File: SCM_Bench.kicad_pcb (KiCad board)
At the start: 4 copper layers, 86 x 145 mm, 330 parts, among them J101 Conn_Coaxial, J102 Conn_Coaxial, J103 Conn_Coaxial, J104 Conn_Coaxial, J105 Conn_Coaxial, J106 Conn_Coaxial, J107 Conn_02x20_Odd_Even, J108 Conn_02x07_Odd_Even, J109 Conn_02x07_Odd_Even, J1601 Conn_01x06, J301 RF_Shield_One_Piece, J401 RF_Shield_One_Piece, J501 RF_Shield_One_Piece, J601 RF_Shield_One_Piece, J701 RF_Shield_One_Piece, J801 RF_Shield_One_Piece, J901 Conn_Coaxial, J902 Conn_Coaxial, J903 Conn_Coaxial, J904 Conn_Coaxial, SW101 SW_Push, U1001 AD9747BCPZ, U1002 SN65LVDS1DBV, U101 ASDMB-xxxMHz, U1101 AD8021, U1201 AD8021, U1301 AD9747BCPZ, U1302 SN65LVDS1DBV, U1401 AD8021, U1501 AD8021, U1601 ICE40HX1K-4K-TQ144, U1602 M25PX32-VMW, U1701 tps6240x, U301 LT6600IS8, U302 LTC2386-18, U303 SN65LVDS1050PW, U401 LT6600IS8, U402 LTC2386-18, U403 SN65LVDS1050PW, U501 LT6600IS8, U502 LTC2386-18, U503 SN65LVDS1050PW, U601 LT6600IS8, U602 LTC2386-18, U603 SN65LVDS1050PW, U701 LT6600IS8, U702 LTC2386-18, U703 SN65LVDS1050PW, U801 LT6600IS8, U802 LTC2386-18, U803 SN65LVDS1050PW

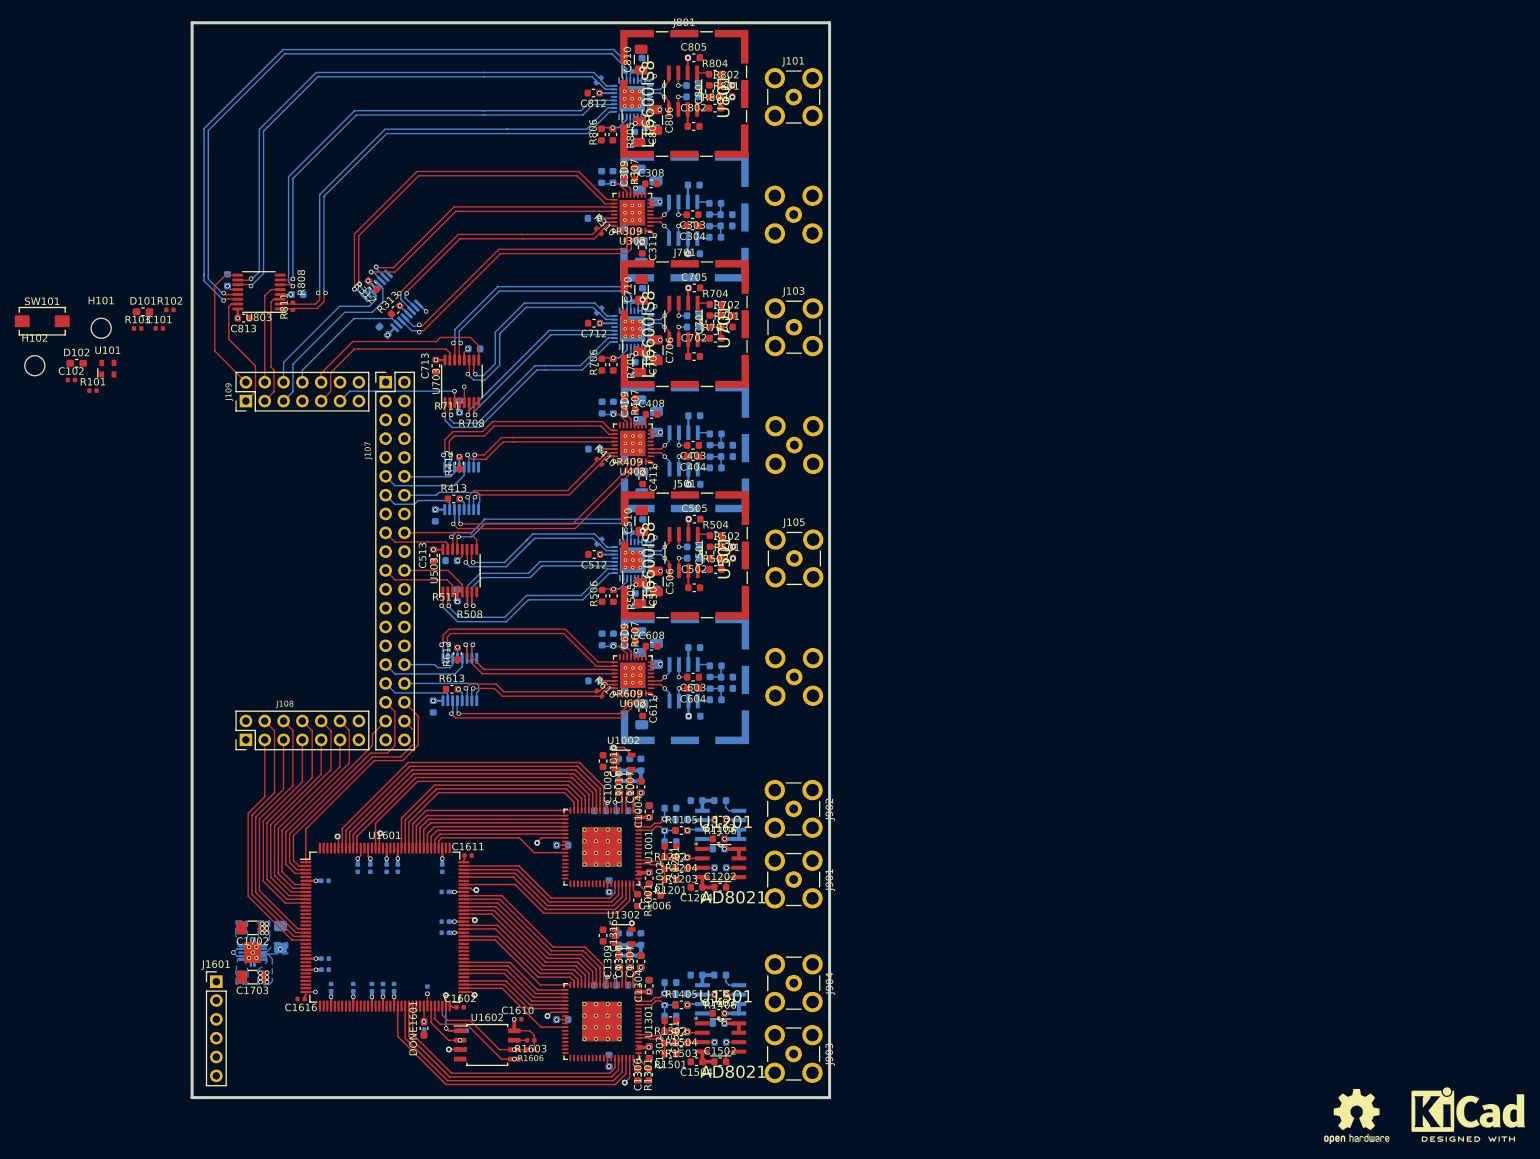
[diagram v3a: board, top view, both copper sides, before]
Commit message: Layout complete, needs silk screen cleanup and few checks
Signed-off-by: Alexis Jeandet <alexis.jeandet@member.fsf.org>
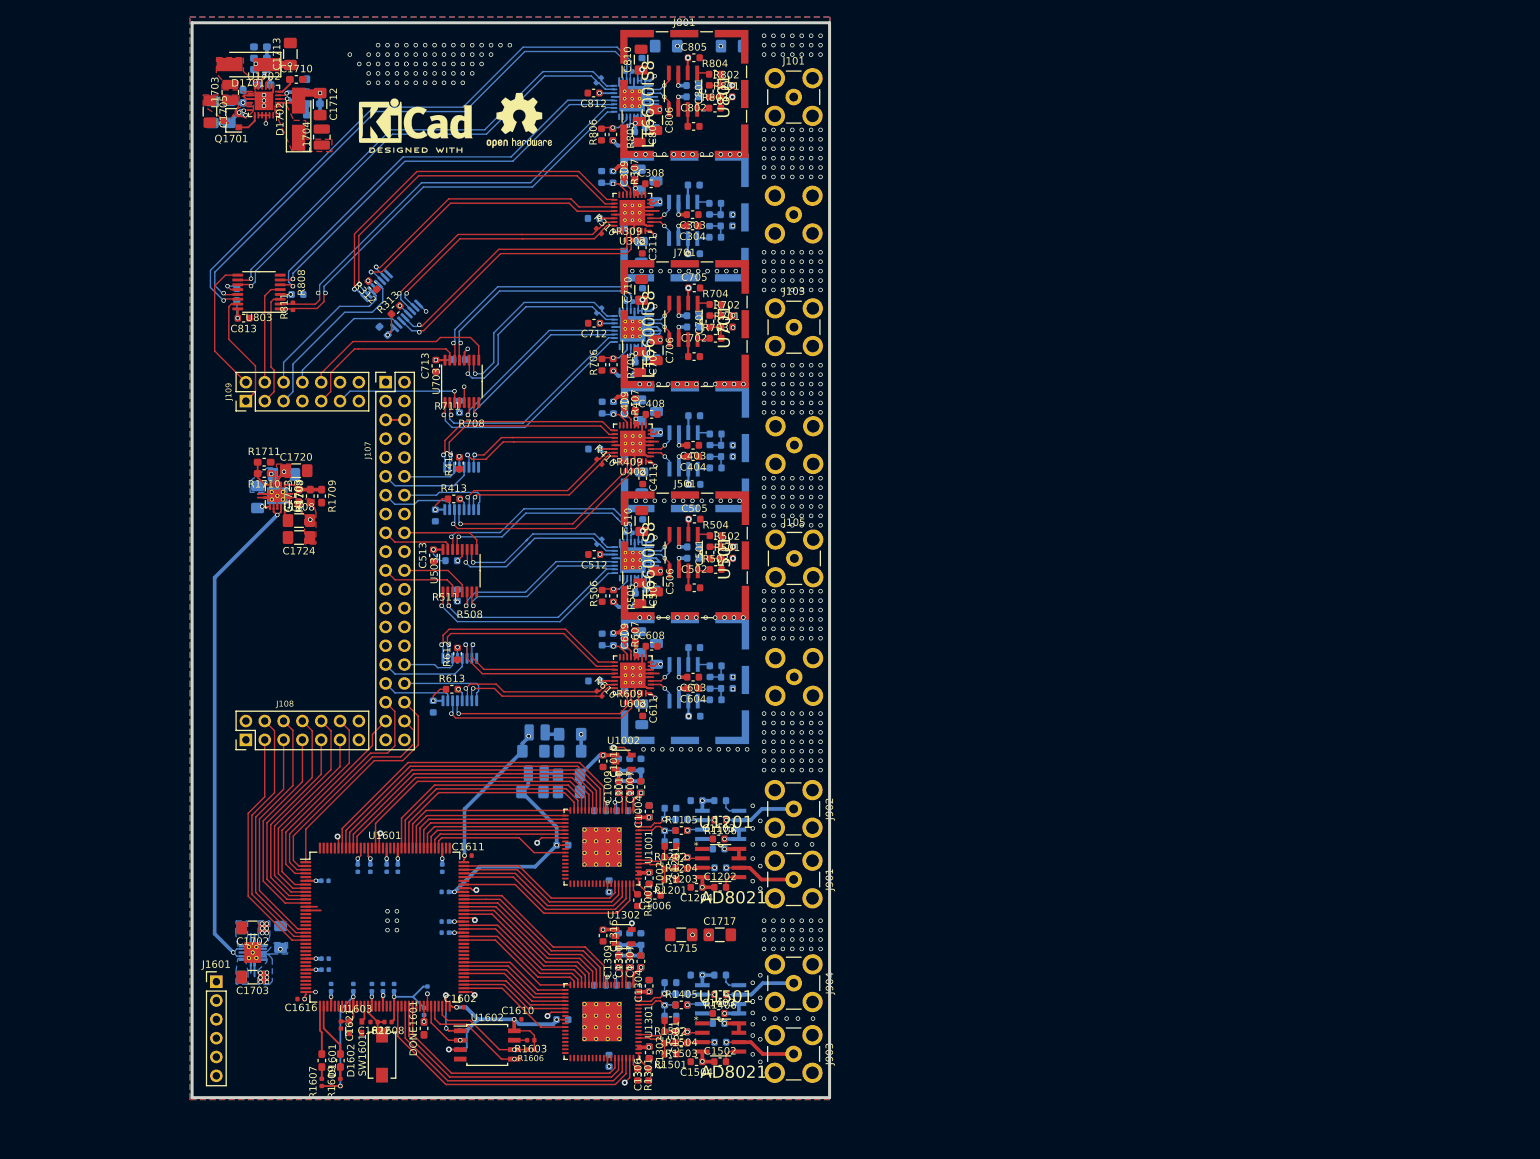
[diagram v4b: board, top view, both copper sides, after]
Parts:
- removed C101, C102: 100nF, Capacitor_SMD:C_0402_1005Metric
- removed D101, D102: LED, Resistor_SMD:R_0603_1608Metric_Pad1.05x0.95mm_HandSolder
- removed H101, H102: MountingHole, MountingHole:MountingHole_2.7mm_M2.5
- removed R101, R102, R103: 2K2, Resistor_SMD:R_0402_1005Metric
- removed SW101: SW_Push, Button_Switch_SMD:SW_SPST_EVQPE1
- removed U101: ASDMB-xxxMHz, Oscillator:Oscillator_SMD_Abracon_ASDMB-4Pin_2.5x2.0mm
- added C1621: 100nF, Capacitor_SMD:C_0402_1005Metric, F.Cu at (80.1, 165.2)
- added C1622: 100nF, Capacitor_SMD:C_0402_1005Metric, F.Cu at (84.5, 164.8)
- added C1704: 4.7uF, Capacitor_SMD:C_1206_3216Metric_Pad1.42x1.75mm_HandSolder, B.Cu at (62.7, 42.0)
- added C1705: 4.7uF, Capacitor_SMD:C_1206_3216Metric_Pad1.42x1.75mm_HandSolder, F.Cu at (62.4, 42.0)
- added C1706: 100nF, Capacitor_SMD:C_0603_1608Metric_Pad1.05x0.95mm_HandSolder, B.Cu at (66.9, 39.9)
- added C1707: C, Capacitor_SMD:C_0603_1608Metric_Pad1.05x0.95mm_HandSolder, B.Cu at (69.7, 38.4)
- added C1708: C, Capacitor_SMD:C_0603_1608Metric_Pad1.05x0.95mm_HandSolder, B.Cu at (75.5, 38.5)
- added C1709: C, Capacitor_SMD:C_0603_1608Metric_Pad1.05x0.95mm_HandSolder, B.Cu at (76.4, 40.9)
- added C1710: C, Capacitor_SMD:C_0603_1608Metric_Pad1.05x0.95mm_HandSolder, F.Cu at (74.1, 37.6)
- added C1711: C, Capacitor_SMD:C_0603_1608Metric_Pad1.05x0.95mm_HandSolder, B.Cu at (69.2, 36.3)
- added C1712: 22uF, Capacitor_SMD:C_1206_3216Metric_Pad1.42x1.75mm_HandSolder, F.Cu at (77.3, 41.0)
- added C1713: 22uF, Capacitor_SMD:C_1206_3216Metric_Pad1.42x1.75mm_HandSolder, F.Cu at (73.3, 34.2)
- added C1714: 4.7uF, Capacitor_SMD:C_1206_3216Metric_Pad1.42x1.75mm_HandSolder, B.Cu at (132.8, 33.1)
- added C1715: 4.7uF, Capacitor_SMD:C_1206_3216Metric_Pad1.42x1.75mm_HandSolder, F.Cu at (126.0, 153.0)
- added C1716: 4.7uF, Capacitor_SMD:C_1206_3216Metric_Pad1.42x1.75mm_HandSolder, B.Cu at (124.0, 33.1)
- added C1717: 4.7uF, Capacitor_SMD:C_1206_3216Metric_Pad1.42x1.75mm_HandSolder, F.Cu at (131.2, 153.0)
- added C1718: 22uF, Capacitor_SMD:C_1206_3216Metric_Pad1.42x1.75mm_HandSolder, B.Cu at (105.9, 133.8)
- added C1719: 22uF, Capacitor_SMD:C_1206_3216Metric_Pad1.42x1.75mm_HandSolder, B.Cu at (110.8, 133.8)
- added C1720: 10uF, Capacitor_SMD:C_1206_3216Metric_Pad1.42x1.75mm_HandSolder, F.Cu at (74.0, 90.4)
- added C1721: 22uF, Capacitor_SMD:C_1206_3216Metric_Pad1.42x1.75mm_HandSolder, B.Cu at (106.0, 128.3)
- added C1722: 22uF, Capacitor_SMD:C_1206_3216Metric_Pad1.42x1.75mm_HandSolder, B.Cu at (111.0, 128.3)
- added C1723: C, Capacitor_SMD:C_0603_1608Metric_Pad1.05x0.95mm_HandSolder, F.Cu at (74.4, 93.9)
- added C1724: 10uF, Capacitor_SMD:C_1206_3216Metric_Pad1.42x1.75mm_HandSolder, F.Cu at (74.4, 99.4)
- added C1725: 10uF, Capacitor_SMD:C_1206_3216Metric_Pad1.42x1.75mm_HandSolder, B.Cu at (72.4, 90.9)
- added D1601: LED, Resistor_SMD:R_0603_1608Metric_Pad1.05x0.95mm_HandSolder, F.Cu at (77.5, 170.0)
- added D1602: LED, Resistor_SMD:R_0603_1608Metric_Pad1.05x0.95mm_HandSolder, F.Cu at (80.0, 170.0)
- added D1701: D_Schottky, Diode_SMD:D_SMA_Handsoldering, F.Cu at (67.6, 35.6)
- added D1702: D_Schottky, Diode_SMD:D_SMA_Handsoldering, F.Cu at (74.4, 43.0)
- added L1703: 4.7uH, Inductor_SMD:L_1008_2520Metric, F.Cu at (65.2, 39.4)
- added L1704: 4.7uH, Inductor_SMD:L_1008_2520Metric, F.Cu at (77.5, 45.4)
- added L1705: 4.7uH, Inductor_SMD:L_1008_2520Metric, B.Cu at (106.4, 131.3)
- added L1706: 4.7uH, Inductor_SMD:L_1008_2520Metric, B.Cu at (106.6, 125.7)
- added L1707: 2.2uH, Inductor_SMD:L_1206_3216Metric_Pad1.42x1.75mm_HandSolder, B.Cu at (68.8, 94.0)
- added L1708: 2.2uH, Inductor_SMD:L_1206_3216Metric_Pad1.42x1.75mm_HandSolder, F.Cu at (74.4, 97.2)
- added Q1701: Q_PMOS_GSD, Package_TO_SOT_SMD:SOT-23, F.Cu at (65.3, 43.2)
- added R1607: 2K2, Resistor_SMD:R_0402_1005Metric, F.Cu at (77.5, 172.9)
- added R1608: 2K2, Resistor_SMD:R_0402_1005Metric, F.Cu at (86.4, 164.8)
- added R1609: 2K2, Resistor_SMD:R_0402_1005Metric, F.Cu at (80.0, 172.9)
- added R1701: 100, Resistor_SMD:R_1206_3216Metric_Pad1.42x1.75mm_HandSolder, B.Cu at (65.0, 42.0)
- added R1702: R, Resistor_SMD:R_0603_1608Metric_Pad1.05x0.95mm_HandSolder, B.Cu at (73.9, 40.2)
- added R1703: R, Resistor_SMD:R_0603_1608Metric_Pad1.05x0.95mm_HandSolder, B.Cu at (76.4, 42.4)
- added R1704: R, Resistor_SMD:R_0603_1608Metric_Pad1.05x0.95mm_HandSolder, B.Cu at (69.2, 34.8)
- added R1705: R, Resistor_SMD:R_0603_1608Metric_Pad1.05x0.95mm_HandSolder, B.Cu at (69.2, 33.2)
- added R1706: 500m, Resistor_SMD:R_1206_3216Metric_Pad1.42x1.75mm_HandSolder, B.Cu at (110.8, 131.5)
- added R1707: 500m, Resistor_SMD:R_1206_3216Metric_Pad1.42x1.75mm_HandSolder, B.Cu at (111.0, 126.0)
- added R1708: R, Resistor_SMD:R_0603_1608Metric_Pad1.05x0.95mm_HandSolder, F.Cu at (75.9, 93.9)
- added R1709: R, Resistor_SMD:R_0603_1608Metric_Pad1.05x0.95mm_HandSolder, F.Cu at (77.5, 93.9)
- added R1710: R, Resistor_SMD:R_0603_1608Metric_Pad1.05x0.95mm_HandSolder, F.Cu at (69.7, 90.8)
- added R1711: R, Resistor_SMD:R_0603_1608Metric_Pad1.05x0.95mm_HandSolder, F.Cu at (69.7, 89.3)
- added SW1601: SW_Push, Button_Switch_SMD:SW_SPST_EVQPE1, F.Cu at (85.6, 169.3)
- added U1603: ASDMB-xxxMHz, Oscillator:Oscillator_SMD_Abracon_ASDMB-4Pin_2.5x2.0mm, F.Cu at (82.1, 165.5)
- added U1702: TPS6513x, Package_DFN_QFN:HVQFN-24-1EP_4x4mm_P0.5mm_EP2.5x2.5mm, F.Cu at (69.7, 40.5)
- added U1703: tps6240x, Package_SON:Texas_S-PVSON-N10_ThermalVias, F.Cu at (71.5, 93.8)
- moved LOGO102 194.8 mm to (90.2, 43.2)
- moved LOGO101 175.5 mm to (104.1, 43.2)
- moved R1602 2.90 mm to (91.3, 163.4), turned to 270 degrees
- moved R713 2.52 mm to (96.0, 75.4), turned to 0 degrees
- moved R813 2.33 mm to (66.0, 66.7), turned to 90 degrees
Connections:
- C1001 pad 2: /Sheet5F420A25/Sheet5F420DB3/AVDD33 -> /3.3V
- C1002 pad 1: /Sheet5F420A25/Sheet5F420DB3/AVDD33 -> /3.3V
- C1003 pad 1: /Sheet5F420A25/Sheet5F420DB3/AVDD33 -> /3.3V
- C1004 pad 1: /Sheet5F420A25/Sheet5F420DB3/AVDD33 -> /3.3V
- C1007 pad 1: /Sheet5F420A25/Sheet5F420DB3/CVDD18 -> /#1.8V
- C1011 pad 1: /Sheet5F420A25/Sheet5F420DB3/CVDD18 -> /#1.8V
- C1013 pad 1: /Sheet5F420A25/Sheet5F420DB3/DVDD18 -> /#1.8V
- C1014 pad 1: /Sheet5F420A25/Sheet5F420DB3/DVDD18 -> /#1.8V
- C1015 pad 1: /Sheet5F420A25/Sheet5F420DB3/AVDD33 -> /3.3V
- C1102 pad 1: /Sheet5F420A25/Sheet5F420DB3/-5V -> /-5V
- C1103 pad 2: /Sheet5F420A25/Sheet5F420DB3/5V -> /5V
- C1104 pad 1: /Sheet5F420A25/Sheet5F420DB3/-5V -> /-5V
- C1202 pad 1: /Sheet5F420A25/Sheet5F420DB3/-5V -> /-5V
- C1203 pad 2: /Sheet5F420A25/Sheet5F420DB3/5V -> /5V
- C1204 pad 1: /Sheet5F420A25/Sheet5F420DB3/-5V -> /-5V
- C1301 pad 2: /Sheet5F420A25/sheet5F604603/AVDD33 -> /3.3V
- C1302 pad 1: /Sheet5F420A25/sheet5F604603/AVDD33 -> /3.3V
- C1303 pad 1: /Sheet5F420A25/sheet5F604603/AVDD33 -> /3.3V
- C1304 pad 1: /Sheet5F420A25/sheet5F604603/AVDD33 -> /3.3V
- C1307 pad 1: /Sheet5F420A25/sheet5F604603/CVDD18 -> /#1.8V
- C1311 pad 1: /Sheet5F420A25/sheet5F604603/CVDD18 -> /#1.8V
- C1313 pad 1: /Sheet5F420A25/sheet5F604603/DVDD18 -> /#1.8V
- C1314 pad 1: /Sheet5F420A25/sheet5F604603/DVDD18 -> /#1.8V
- C1315 pad 1: /Sheet5F420A25/sheet5F604603/AVDD33 -> /3.3V
- C1402 pad 1: /Sheet5F420A25/sheet5F604603/-5V -> /-5V
- C1403 pad 2: /Sheet5F420A25/sheet5F604603/5V -> /5V
- C1404 pad 1: /Sheet5F420A25/sheet5F604603/-5V -> /-5V
- C1502 pad 1: /Sheet5F420A25/sheet5F604603/-5V -> /-5V
- C1503 pad 2: /Sheet5F420A25/sheet5F604603/5V -> /5V
- C1504 pad 1: /Sheet5F420A25/sheet5F604603/-5V -> /-5V
- C1611 pad 1: /Sheet5F420A25/#2.5V -> /#2.5V
- C303 pad 2: /Sheet5F3E1819/Sheet5F3E1AE4/V- -> /-5V
- C304 pad 2: /Sheet5F3E1819/Sheet5F3E1AE4/V+ -> /5V
- C307 pad 1: /Sheet5F3E1819/Sheet5F3E1AE4/VDD -> /5V
- C309 pad 1: /Sheet5F3E1819/Sheet5F3E1AE4/VDD -> /5V
- C310 pad 1: /Sheet5F3E1819/Sheet5F3E1AE4/VDDL -> /2.5V
- C311 pad 1: /Sheet5F3E1819/Sheet5F3E1AE4/VDDL -> /2.5V
- C312 pad 1: /Sheet5F3E1819/Sheet5F3E1AE4/OVDD -> /#2.5V
- C313 pad 2: /Sheet5F3E1819/Sheet5F3E1AE4/OVDD -> /#2.5V
- C403 pad 2: /Sheet5F3E1819/sheet5F7670FC/V- -> /-5V
- C404 pad 2: /Sheet5F3E1819/sheet5F7670FC/V+ -> /5V
- C407 pad 1: /Sheet5F3E1819/sheet5F7670FC/VDD -> /5V
- C409 pad 1: /Sheet5F3E1819/sheet5F7670FC/VDD -> /5V
- C410 pad 1: /Sheet5F3E1819/sheet5F7670FC/VDDL -> /2.5V
- C411 pad 1: /Sheet5F3E1819/sheet5F7670FC/VDDL -> /2.5V
- C412 pad 1: /Sheet5F3E1819/sheet5F7670FC/OVDD -> /#2.5V
- C413 pad 2: /Sheet5F3E1819/sheet5F7670FC/OVDD -> /#2.5V
- C503 pad 2: /Sheet5F3E1819/sheet5F767499/V- -> /-5V
- C504 pad 2: /Sheet5F3E1819/sheet5F767499/V+ -> /5V
- C507 pad 1: /Sheet5F3E1819/sheet5F767499/VDD -> /5V
- C509 pad 1: /Sheet5F3E1819/sheet5F767499/VDD -> /5V
- C510 pad 1: /Sheet5F3E1819/sheet5F767499/VDDL -> /2.5V
- C511 pad 1: /Sheet5F3E1819/sheet5F767499/VDDL -> /2.5V
- C512 pad 1: /Sheet5F3E1819/sheet5F767499/OVDD -> /#2.5V
- C513 pad 2: /Sheet5F3E1819/sheet5F767499/OVDD -> /#2.5V
- C603 pad 2: /Sheet5F3E1819/sheet5F766F53/V- -> /-5V
- C604 pad 2: /Sheet5F3E1819/sheet5F766F53/V+ -> /5V
- C607 pad 1: /Sheet5F3E1819/sheet5F766F53/VDD -> /5V
- C609 pad 1: /Sheet5F3E1819/sheet5F766F53/VDD -> /5V
- C610 pad 1: /Sheet5F3E1819/sheet5F766F53/VDDL -> /2.5V
- C611 pad 1: /Sheet5F3E1819/sheet5F766F53/VDDL -> /2.5V
- C612 pad 1: /Sheet5F3E1819/sheet5F766F53/OVDD -> /#2.5V
- C613 pad 2: /Sheet5F3E1819/sheet5F766F53/OVDD -> /#2.5V
- C703 pad 2: /Sheet5F3E1819/sheet5F76778E/V- -> /-5V
- C704 pad 2: /Sheet5F3E1819/sheet5F76778E/V+ -> /5V
- C707 pad 1: /Sheet5F3E1819/sheet5F76778E/VDD -> /2.5V
- C709 pad 1: /Sheet5F3E1819/sheet5F76778E/VDD -> /2.5V
- C710 pad 1: /Sheet5F3E1819/sheet5F76778E/VDDL -> /5V
- C711 pad 1: /Sheet5F3E1819/sheet5F76778E/VDDL -> /5V
- C712 pad 1: /Sheet5F3E1819/sheet5F76778E/OVDD -> /#2.5V
- C713 pad 2: /Sheet5F3E1819/sheet5F76778E/OVDD -> /#2.5V
- C803 pad 2: /Sheet5F3E1819/sheet5F7672A2/V- -> /-5V
- C804 pad 2: /Sheet5F3E1819/sheet5F7672A2/V+ -> /5V
- C807 pad 1: /Sheet5F3E1819/sheet5F7672A2/VDD -> /5V
- C809 pad 1: /Sheet5F3E1819/sheet5F7672A2/VDD -> /5V
- C810 pad 1: /Sheet5F3E1819/sheet5F7672A2/VDDL -> /2.5V
- C811 pad 1: /Sheet5F3E1819/sheet5F7672A2/VDDL -> /2.5V
- C812 pad 1: /Sheet5F3E1819/sheet5F7672A2/OVDD -> /#2.5V
- C813 pad 2: /Sheet5F3E1819/sheet5F7672A2/OVDD -> /#2.5V
- J107 pad 5: /3.3V -> /USB_3.3V
- J107 pad 6: /3.3V -> /USB_3.3V
- R1004 pad 2: /Sheet5F420A25/Sheet5F420DB3/CVDD18 -> /#1.8V
- R1304 pad 2: /Sheet5F420A25/sheet5F604603/CVDD18 -> /#1.8V
- R305 pad 2: /Sheet5F3E1819/Sheet5F3E1AE4/OVDD -> /#2.5V
- R307 pad 1: /Sheet5F3E1819/Sheet5F3E1AE4/OVDD -> /#2.5V
- R313 pad 1: /Sheet5F3E1819/Sheet5F3E1AE4/OVDD -> /#2.5V
- R405 pad 2: /Sheet5F3E1819/sheet5F7670FC/OVDD -> /#2.5V
- R407 pad 1: /Sheet5F3E1819/sheet5F7670FC/OVDD -> /#2.5V
- R413 pad 1: /Sheet5F3E1819/sheet5F7670FC/OVDD -> /#2.5V
- R505 pad 2: /Sheet5F3E1819/sheet5F767499/OVDD -> /#2.5V
- R507 pad 1: /Sheet5F3E1819/sheet5F767499/OVDD -> /#2.5V
- R513 pad 1: /Sheet5F3E1819/sheet5F767499/OVDD -> /#2.5V
- R605 pad 2: /Sheet5F3E1819/sheet5F766F53/OVDD -> /#2.5V
- R607 pad 1: /Sheet5F3E1819/sheet5F766F53/OVDD -> /#2.5V
- R613 pad 1: /Sheet5F3E1819/sheet5F766F53/OVDD -> /#2.5V
- R705 pad 2: /Sheet5F3E1819/sheet5F76778E/OVDD -> /#2.5V
- R707 pad 1: /Sheet5F3E1819/sheet5F76778E/OVDD -> /#2.5V
- R713 pad 1: /Sheet5F3E1819/sheet5F76778E/OVDD -> /#2.5V
- R805 pad 2: /Sheet5F3E1819/sheet5F7672A2/OVDD -> /#2.5V
- R807 pad 1: /Sheet5F3E1819/sheet5F7672A2/OVDD -> /#2.5V
- R813 pad 1: /Sheet5F3E1819/sheet5F7672A2/OVDD -> /#2.5V
- U1001 pad 1: /Sheet5F420A25/Sheet5F420DB3/CVDD18 -> /#1.8V
- U1001 pad 47: /Sheet5F420A25/Sheet5F420DB3/DVDD18 -> /#1.8V
- U1001 pad 56: /Sheet5F420A25/Sheet5F420DB3/AVDD33 -> /3.3V
- U1001 pad 57: /Sheet5F420A25/Sheet5F420DB3/AVDD33 -> /3.3V
- U1001 pad 6: /Sheet5F420A25/Sheet5F420DB3/CVDD18 -> /#1.8V
- U1001 pad 71: /Sheet5F420A25/Sheet5F420DB3/AVDD33 -> /3.3V
- U1001 pad 72: /Sheet5F420A25/Sheet5F420DB3/AVDD33 -> /3.3V
- U1001 pad 8: /Sheet5F420A25/Sheet5F420DB3/DVDD18 -> /#1.8V
- U1002 pad 1: /Sheet5F420A25/Sheet5F420DB3/AVDD33 -> /3.3V
- U1101 pad 4: /Sheet5F420A25/Sheet5F420DB3/-5V -> /-5V
- U1101 pad 7: /Sheet5F420A25/Sheet5F420DB3/5V -> /5V
- U1101 pad 8: /Sheet5F420A25/Sheet5F420DB3/5V -> /5V
- U1201 pad 4: /Sheet5F420A25/Sheet5F420DB3/-5V -> /-5V
- U1201 pad 7: /Sheet5F420A25/Sheet5F420DB3/5V -> /5V
- U1201 pad 8: /Sheet5F420A25/Sheet5F420DB3/5V -> /5V
- U1301 pad 1: /Sheet5F420A25/sheet5F604603/CVDD18 -> /#1.8V
- U1301 pad 47: /Sheet5F420A25/sheet5F604603/DVDD18 -> /#1.8V
- U1301 pad 56: /Sheet5F420A25/sheet5F604603/AVDD33 -> /3.3V
- U1301 pad 57: /Sheet5F420A25/sheet5F604603/AVDD33 -> /3.3V
- U1301 pad 6: /Sheet5F420A25/sheet5F604603/CVDD18 -> /#1.8V
- U1301 pad 71: /Sheet5F420A25/sheet5F604603/AVDD33 -> /3.3V
- U1301 pad 72: /Sheet5F420A25/sheet5F604603/AVDD33 -> /3.3V
- U1301 pad 8: /Sheet5F420A25/sheet5F604603/DVDD18 -> /#1.8V
- U1302 pad 1: /Sheet5F420A25/sheet5F604603/AVDD33 -> /3.3V
- U1401 pad 4: /Sheet5F420A25/sheet5F604603/-5V -> /-5V
- U1401 pad 7: /Sheet5F420A25/sheet5F604603/5V -> /5V
- U1401 pad 8: /Sheet5F420A25/sheet5F604603/5V -> /5V
- U1501 pad 4: /Sheet5F420A25/sheet5F604603/-5V -> /-5V
- U1501 pad 7: /Sheet5F420A25/sheet5F604603/5V -> /5V
- U1501 pad 8: /Sheet5F420A25/sheet5F604603/5V -> /5V
- U1601 pad 108: /Sheet5F420A25/#2.5V -> /#2.5V
- U1601 pad 37: (no net) -> /Sheet5F420A25/sheet5F62EEDA/LED1
- U1601 pad 38: (no net) -> /Sheet5F420A25/sheet5F62EEDA/LED2
- U1601 pad 49: (no net) -> /Sheet5F420A25/sheet5F62EEDA/FPGA_CLK
- U1601 pad 50: (no net) -> /Sheet5F420A25/sheet5F62EEDA/BP
- U301 pad 3: /Sheet5F3E1819/Sheet5F3E1AE4/V+ -> /5V
- U301 pad 6: /Sheet5F3E1819/Sheet5F3E1AE4/V- -> /-5V
- U302 pad 11: /Sheet5F3E1819/Sheet5F3E1AE4/VDD -> /5V
- U302 pad 12: /Sheet5F3E1819/Sheet5F3E1AE4/VDD -> /5V
- U302 pad 22: /Sheet5F3E1819/Sheet5F3E1AE4/OVDD -> /#2.5V
- U302 pad 30: /Sheet5F3E1819/Sheet5F3E1AE4/VDDL -> /2.5V
- U302 pad 31: /Sheet5F3E1819/Sheet5F3E1AE4/VDDL -> /2.5V
- U303 pad 16: /Sheet5F3E1819/Sheet5F3E1AE4/OVDD -> /#2.5V
- U401 pad 3: /Sheet5F3E1819/sheet5F7670FC/V+ -> /5V
- U401 pad 6: /Sheet5F3E1819/sheet5F7670FC/V- -> /-5V
- U402 pad 11: /Sheet5F3E1819/sheet5F7670FC/VDD -> /5V
- U402 pad 12: /Sheet5F3E1819/sheet5F7670FC/VDD -> /5V
- U402 pad 22: /Sheet5F3E1819/sheet5F7670FC/OVDD -> /#2.5V
- U402 pad 30: /Sheet5F3E1819/sheet5F7670FC/VDDL -> /2.5V
- U402 pad 31: /Sheet5F3E1819/sheet5F7670FC/VDDL -> /2.5V
- U403 pad 16: /Sheet5F3E1819/sheet5F7670FC/OVDD -> /#2.5V
- U501 pad 3: /Sheet5F3E1819/sheet5F767499/V+ -> /5V
- U501 pad 6: /Sheet5F3E1819/sheet5F767499/V- -> /-5V
- U502 pad 11: /Sheet5F3E1819/sheet5F767499/VDD -> /5V
- U502 pad 12: /Sheet5F3E1819/sheet5F767499/VDD -> /5V
- U502 pad 22: /Sheet5F3E1819/sheet5F767499/OVDD -> /#2.5V
- U502 pad 30: /Sheet5F3E1819/sheet5F767499/VDDL -> /2.5V
- U502 pad 31: /Sheet5F3E1819/sheet5F767499/VDDL -> /2.5V
- U503 pad 16: /Sheet5F3E1819/sheet5F767499/OVDD -> /#2.5V
- U601 pad 3: /Sheet5F3E1819/sheet5F766F53/V+ -> /5V
- U601 pad 6: /Sheet5F3E1819/sheet5F766F53/V- -> /-5V
- U602 pad 11: /Sheet5F3E1819/sheet5F766F53/VDD -> /5V
- U602 pad 12: /Sheet5F3E1819/sheet5F766F53/VDD -> /5V
- U602 pad 22: /Sheet5F3E1819/sheet5F766F53/OVDD -> /#2.5V
- U602 pad 30: /Sheet5F3E1819/sheet5F766F53/VDDL -> /2.5V
- U602 pad 31: /Sheet5F3E1819/sheet5F766F53/VDDL -> /2.5V
- U603 pad 16: /Sheet5F3E1819/sheet5F766F53/OVDD -> /#2.5V
- U701 pad 3: /Sheet5F3E1819/sheet5F76778E/V+ -> /5V
- U701 pad 6: /Sheet5F3E1819/sheet5F76778E/V- -> /-5V
- U702 pad 11: /Sheet5F3E1819/sheet5F76778E/VDD -> /2.5V
- U702 pad 12: /Sheet5F3E1819/sheet5F76778E/VDD -> /2.5V
- U702 pad 22: /Sheet5F3E1819/sheet5F76778E/OVDD -> /#2.5V
- U702 pad 30: /Sheet5F3E1819/sheet5F76778E/VDDL -> /5V
- U702 pad 31: /Sheet5F3E1819/sheet5F76778E/VDDL -> /5V
- U703 pad 16: /Sheet5F3E1819/sheet5F76778E/OVDD -> /#2.5V
- U801 pad 3: /Sheet5F3E1819/sheet5F7672A2/V+ -> /5V
- U801 pad 6: /Sheet5F3E1819/sheet5F7672A2/V- -> /-5V
- U802 pad 11: /Sheet5F3E1819/sheet5F7672A2/VDD -> /5V
- U802 pad 12: /Sheet5F3E1819/sheet5F7672A2/VDD -> /5V
- U802 pad 22: /Sheet5F3E1819/sheet5F7672A2/OVDD -> /#2.5V
- U802 pad 30: /Sheet5F3E1819/sheet5F7672A2/VDDL -> /2.5V
- U802 pad 31: /Sheet5F3E1819/sheet5F7672A2/VDDL -> /2.5V
- U803 pad 16: /Sheet5F3E1819/sheet5F7672A2/OVDD -> /#2.5V
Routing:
- net /#2.5V: track 0.00 -> 272.0 mm, vias 0 -> 21
- net GND: track 0.00 -> 180.3 mm, vias 0 -> 479
- net /USB_5V: track 10.3 -> 169.8 mm, vias 2 -> 8
- net /#1.8V: track 0.00 -> 152.6 mm, vias 0 -> 9
- net /5V: track 0.00 -> 110.9 mm, vias 0 -> 20
- net /-5V: track 0.00 -> 96.7 mm, vias 0 -> 13
- net VCCIO_0: track 29.1 -> 105.3 mm, vias 18 -> 20
- net /2.5V: track 0.00 -> 24.2 mm, vias 0 -> 7
- net /Sheet5F3E1819/CH4_IN-: track 0.00 -> 21.4 mm, vias 0 -> 1
- net /Sheet5F3E1819/CH1_IN-: track 0.00 -> 21.4 mm
- net /Sheet5F3E1819/CH5_IN-: track 0.00 -> 21.4 mm
- net /Sheet5F3E1819/CH6_IN-: track 0.00 -> 21.3 mm, vias 0 -> 1
- net /Sheet5F3E1819/CH3_IN-: track 0.00 -> 21.3 mm, vias 0 -> 1
- net /3.3V: track 0.00 -> 17.5 mm, vias 0 -> 6
- net /Sheet5F3E1819/sheet5F7672A2/CNV+: track 91.9 -> 79.7 mm
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- added copper zone on B.Cu, net /#1.8V
- added copper zone on F.Cu, net /#2.5V
- added copper zone on In1.Cu, net /-5V
- added copper zone on In1.Cu, net /2.5V
- added copper zone on In1.Cu, net /3.3V
- added copper zone on In2.Cu, net /5V
- added copper zone on F.Cu, net /USB_5V
- added copper zone on In1.Cu, net /USB_5V
- added copper zone on B.Cu, net GND
- added copper zone on F.Cu, net GND
- added copper zone on In1.Cu, net GND
- added copper zone on In2.Cu, net GND
- added copper zone on F.Cu, net Net-(C1705-Pad1)
- added copper zone on F.Cu, net Net-(D1701-Pad2)
- added copper zone on F.Cu, net Net-(D1702-Pad1)
- added copper zone on In2.Cu, net VCC
- added copper zone on In1.Cu, net VCCIO_0

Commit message: PCB ready for review
Signed-off-by: Alexis Jeandet <alexis.jeandet@member.fsf.org>
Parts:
- added J110: Conn_Coaxial, Connector_Coaxial:SMB_Jack_Vertical, F.Cu at (68.1, 107.0)
- added J111: Conn_Coaxial, Connector_Coaxial:SMB_Jack_Vertical, F.Cu at (79.0, 107.0)
- moved L1707 5.33 mm to (68.8, 88.6)
- moved C1720 5.33 mm to (74.0, 85.1)
- moved C1724 5.33 mm to (74.4, 94.1)
- moved C1725 5.33 mm to (72.4, 85.6)
- moved L1708 5.33 mm to (74.4, 91.8)
- moved R1710 5.33 mm to (69.7, 85.5)
- moved R1711 5.33 mm to (69.7, 83.9)
- moved U1703 5.33 mm to (71.5, 88.5)
- moved C1723 5.33 mm to (74.4, 88.5)
- moved R1708 5.33 mm to (75.9, 88.5)
- moved R1709 5.33 mm to (77.5, 88.5)
- moved C1701 0.09 mm to (72.0, 153.3)
- moved C711 0.08 mm to (120.8, 66.7)
- moved C311 0.05 mm to (120.7, 60.3)
- moved C408 0.05 mm to (122.0, 82.8)
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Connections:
- J107 pad 19: (no net) -> /IOB_15
- J107 pad 23: (no net) -> /IOB_11
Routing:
- net GND: track 180.3 -> 227.2 mm
- net /IOB_15: track 0.00 -> 22.4 mm
- net /IOB_11: track 0.00 -> 7.32 mm
- net /#1.8V: track 152.6 -> 156.4 mm
- net /FLASH_SS: track 114.5 -> 111.6 mm
- net /FLASH_MOSI: track 133.7 -> 130.7 mm
- net /FLASH_~CRESET: track 106.6 -> 103.6 mm
- net /FLASH_MISO: track 115.2 -> 112.2 mm
- net /FLASH_CLK: track 132.9 -> 129.9 mm
- net /USB_5V: track 169.8 -> 171.2 mm
- net VCCIO_0: vias 20 -> 18
- net VCC: vias 15 -> 13
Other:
- board text added: "Done"

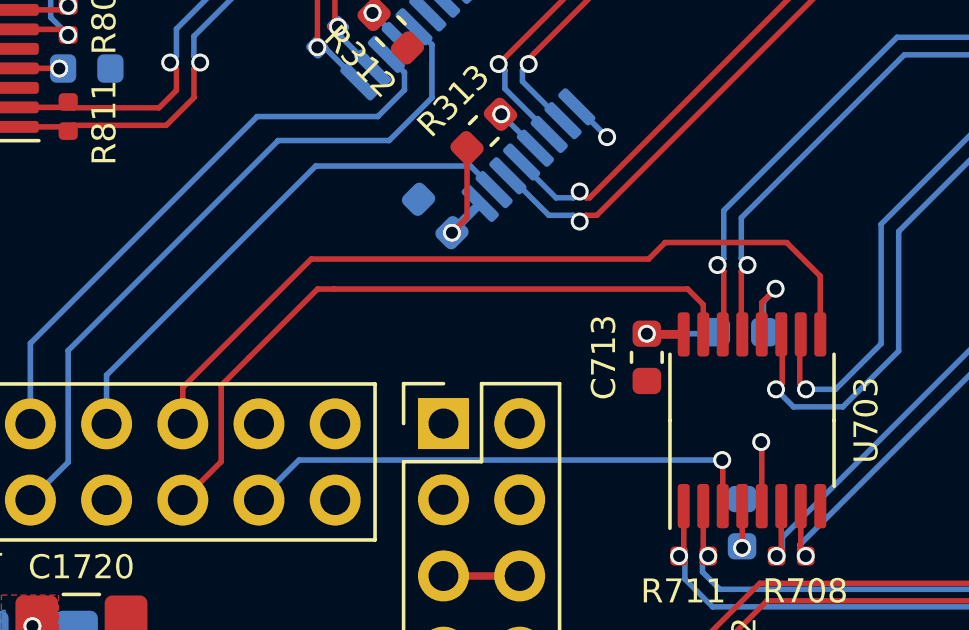
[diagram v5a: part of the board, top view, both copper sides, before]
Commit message: Fixed mistake on one ADC chan power line
Signed-off-by: Alexis Jeandet <alexis.jeandet@member.fsf.org>
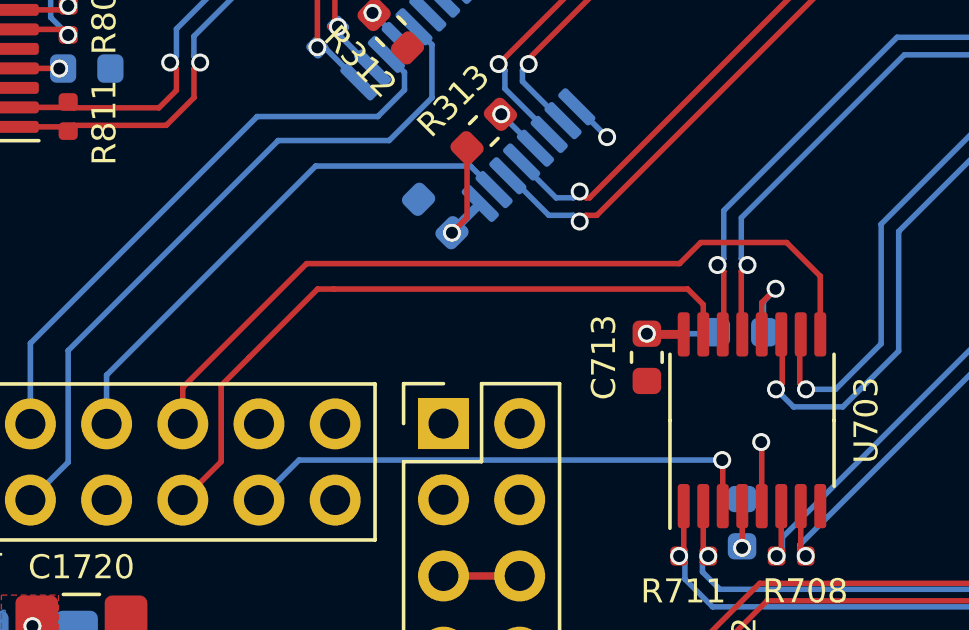
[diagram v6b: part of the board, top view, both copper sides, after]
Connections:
- C707 pad 1: /2.5V -> /5V
- C709 pad 1: /2.5V -> /5V
- C710 pad 1: /5V -> /2.5V
- C711 pad 1: /5V -> /2.5V
- U702 pad 11: /2.5V -> /5V
- U702 pad 12: /2.5V -> /5V
- U702 pad 30: /5V -> /2.5V
- U702 pad 31: /5V -> /2.5V
